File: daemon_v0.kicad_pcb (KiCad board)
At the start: 4 copper layers, 91.5 x 53 mm, 338 parts, among them J1 Battery PTC 2A Fuse, J10 USB-A♂ Charge Port 4, J11 USB-C♀ Main Port 5, J12 WAGO 4P Field Terminal, J13 USB-C♀ Goobay Bridge, J14 RJ45 MagJack, J15 TRRS 3.5mm Jack, J16 Speaker JST, J17 Analog-In, J2 10mΩ Current Sense, J3 40-Pin Radxa Header, J4 AUX GPIO Breakout, J6 ST7789 SPI Display, J7 USB-C♂ Plug → Radxa (KEY), J8 USB-A♀ Host Port 2, J9 USB-A♀ Host Port 3, K1 G6K-2F-Y, Q1 BC857 Dummy Load PNP, Q2 BSS84 Wake PMOS, Q3 2N7002 PMIC Kill NMOS, Q4 AO3400A IR Drive NMOS, Q5 AO3400A, SW1 Power Button, SW2 5-Way Nav Switch, U1 IP5328P PMIC, U10 MAX98357A I2S Amp, U11 ISO1212 Dual Isolator, U12 ESD USB Port1, U13 INMP441 Mic Left, U14 SL2.1A USB Hub 2, U15 SY6280 Port4 USB-A♂, U16 ESD USB Port2, U17 ESD USB Port3, U18 ESD USB Port4, U19 ESD USB Port5, U2 AP2112K 3.3V LDO, U20 ESD Goobay Bridge, U21 PCF8574 I2C GPIO Exp, U22 SY6280 Port5 USB-C♀, U23 3.3→5V Level Shifter, U24 INMP441 Mic Right, U25 ESD9B5.0ST5G, U26 ESD9B5.0ST5G, U27 NAU88C22, U28 ADS1115, U29 SP3485, U3 SL2.1A USB Hub 1, U30 TSOP38238, U31 ATECC608B, U32 74LVC04A, U33 TS3USB221, U34 TS3USB221, U35 TS3USB221, U36 TS3USB221, U37 TS3USB221, U4 SY6280 Port1 Radxa Key, U5 SY6280 Port2 USB-A♀, U6 SY6280 Port3 USB-A♀, U7 NE555 Heartbeat Timer, U8 CC1101 Sub-GHz Radio, U9 RTL8152B Ethernet, Y1 12MHz Hub1 Xtal, Y2 12MHz Hub2 Xtal, Y3 27MHz CC1101 Xtal, Y4 25MHz Ethernet Xtal

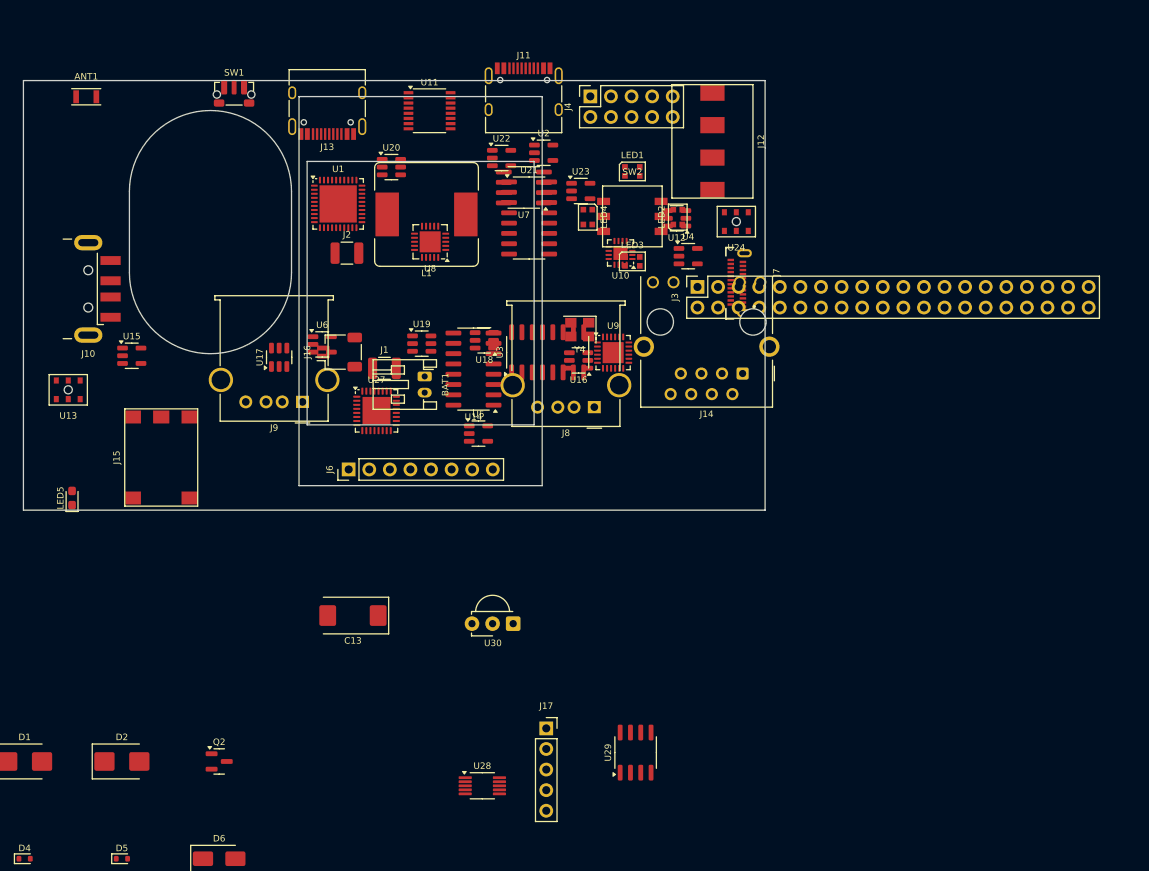
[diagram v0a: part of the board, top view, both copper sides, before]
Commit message: fix: restore component flip/side from screenshot2 — 23 on back side
Components correctly placed on B.Cu (back): BAT1, J3, J7-J11, J14-J16,
L1, LED5, SW1, U7, U10, U12, U13, U16, U18, U24, U30, Y4, C13.

Co-Authored-By: Claude Opus 4.6 (1M context) <noreply@anthropic.com>
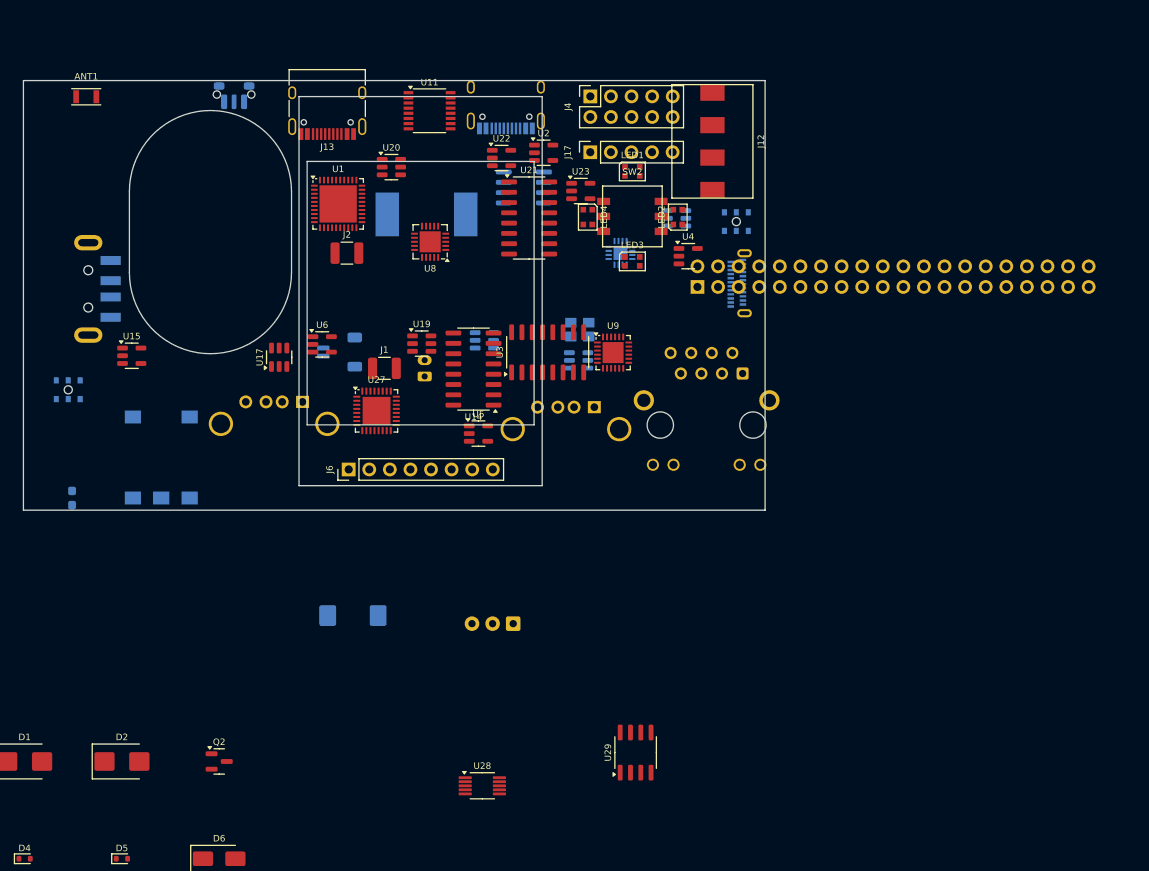
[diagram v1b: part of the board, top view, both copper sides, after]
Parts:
- BAT1, C13, J10, J11, J14, J15, J16, J3, J7, J8, J9, L1, LED5, SW1, U10, U12, U13, U16, U18, U24, U30, U7, Y4: moved to B.Cu
- moved J17 71.3 mm to (129.4, 108.8), turned to 90 degrees
- moved J11 2.30 mm to (119.0, 101.9)
- turned BAT1 to 90 degrees
- turned J15 to -90 degrees
- turned J16 to -90 degrees
- turned J3 to -90 degrees
- turned J7 to 90 degrees
- turned LED5 to -90 degrees

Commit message: fix: screenshot3 sync + 3D model paths + J6 back to female socket
- Applied all 338 placements from screenshot3 (83 back-side components)
- Fixed 3D model paths in custom footprints (KIPRJMOD/lib/3dmodels/)
- J6 screen connector: back to PinSocket (female, on back side)
- 4585 drawings preserved from screenshot3

4 custom 3D models now resolve correctly:
  Antenna, RJ45 MagJack, Alps nav switch, USB-C receptacle

Still need 3D models (not freely downloadable):
  USB-C plug, INMP441, TRRS jack, WAGO, JST speaker

Co-Authored-By: Claude Opus 4.6 (1M context) <noreply@anthropic.com>
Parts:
- C101, C102, C114, C115, C19, C51, C55, C63, C65, C71, C72, C75, C78, C79, C83, C89, C90, D1, D14, D15, D2, D21, D22, D23, D24, D25, D26, FB1, K1, L3, L7, Q2, Q4, R18, R34, R35, R36, R37, R38, R39, R40, R42, R43, R45, R46, R47, R49, R55, R56, R58, R62, R63, R64, R65, R71, R72, R73, R74, U26, U28, U29: moved to B.Cu
- J6: footprint PinHeader_1x08_P2.54mm_Vertical -> PinSocket_1x08_P2.54mm_Vertical
- LED5: moved to F.Cu
- moved R71 500.3 mm to (124.7, 104.4), turned to 180 degrees
- moved R70 496.6 mm to (124.2, 105.9), turned to 180 degrees
- moved R72 493.9 mm to (139.5, 109.0), turned to 90 degrees
- moved R69 486.1 mm to (137.7, 110.6)
- moved R74 485.8 mm to (141.9, 106.8), turned to 180 degrees
- moved R68 485.5 mm to (131.1, 110.8)
- moved R73 485.0 mm to (139.9, 106.7), turned to 180 degrees
- moved R67 483.9 mm to (128.9, 111.0)
- moved C123 475.5 mm to (72.0, 146.3), turned to 180 degrees
- moved C125 474.6 mm to (86.0, 148.0)
- moved C124 473.0 mm to (72.5, 152.0), turned to 90 degrees
- moved R75 467.6 mm to (71.5, 143.3)
- moved C122 466.7 mm to (73.5, 152.0), turned to 90 degrees
- moved C121 464.6 mm to (71.5, 152.0), turned to 90 degrees
- moved R66 462.6 mm to (68.5, 141.5), turned to 90 degrees
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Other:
- board size 91.5 x 53 mm -> 86 x 53 mm
